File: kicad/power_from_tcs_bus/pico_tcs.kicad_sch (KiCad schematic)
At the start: 14 parts, among them J1 TCS In, J2 Conn_01x20_Male, J3 Conn_01x20_Male, J4 Keypad, J5 Display, U1 L7805, U2 ULN2003

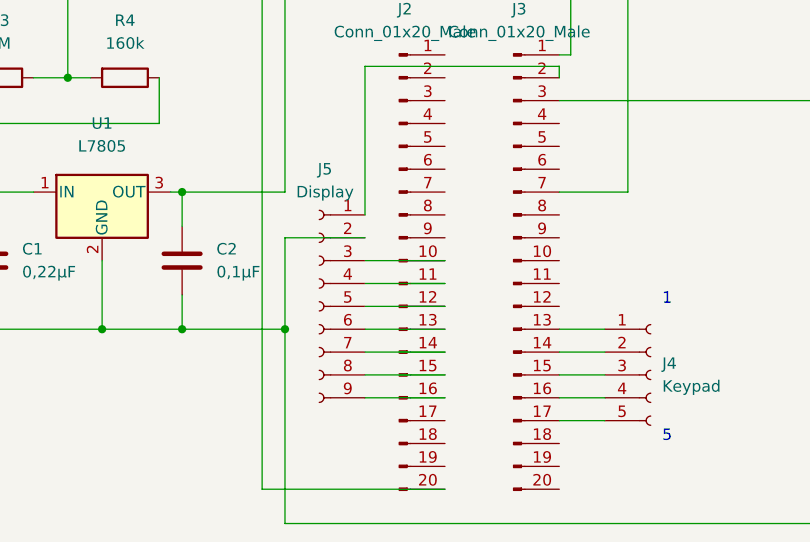
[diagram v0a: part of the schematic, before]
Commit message: Dateien hochladen nach „kicad/power_from_tcs_bus“
fixed bug in connection between display and pico
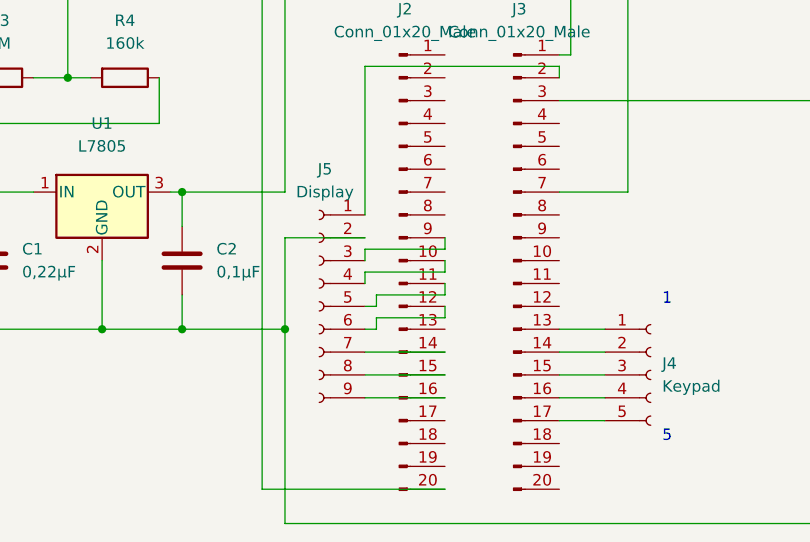
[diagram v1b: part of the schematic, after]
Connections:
- net at J5.3 (Pin_3): now also J2.9 (Pin_9); no longer J2.10 (Pin_10)
- net at J5.4 (Pin_4): now also J2.10 (Pin_10); no longer J2.11 (Pin_11)
- net at J5.5 (Pin_5): now also J2.11 (Pin_11); no longer J2.12 (Pin_12)
- net at J5.6 (Pin_6): now also J2.12 (Pin_12); no longer J2.13 (Pin_13)
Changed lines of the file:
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@@
+    (stroke (width 0) (type default) (color 0 0 0 0))
+  )
+  (wire (pts (xy 128.27 59.69) (xy 128.27 60.96))
     (stroke (width 0) (type default) (color 0 0 0 0))
   )
@@
   )
   (wire (pts (xy 110.49 69.85) (xy 99.06 69.85))
-    (stroke (width 0) (type default) (color 0 0 0 0))
-  )
-  (wire (pts (xy 119.38 69.85) (xy 128.27 69.85))
     (stroke (width 0) (type default) (color 0 0 0 0))
   )
@@
     (stroke (width 0) (type default) (color 0 0 0 0))
   )
+  (wire (pts (xy 119.38 77.47) (xy 128.27 77.47))
+    (stroke (width 0) (type default) (color 0 0 0 0))
+  )
   (wire (pts (xy 66.04 46.99) (xy 66.04 62.23))
     (stroke (width 0) (type default) (color 0 0 0 0))
   )
   (wire (pts (xy 66.04 62.23) (xy 71.12 62.23))
+    (stroke (width 0) (type default) (color 0 0 0 0))
+  )
+  (wire (pts (xy 119.38 69.85) (xy 120.65 69.85))
+    (stroke (width 0) (type default) (color 0 0 0 0))
+  )
+  (wire (pts (xy 119.38 64.77) (xy 119.38 63.5))
+    (stroke (width 0) (type default) (color 0 0 0 0))
+  )
+  (wire (pts (xy 119.38 74.93) (xy 128.27 74.93))
     (stroke (width 0) (type default) (color 0 0 0 0))
   )
@@
     (stroke (width 0) (type default) (color 0 0 0 0))
   )
-  (wire (pts (xy 119.38 62.23) (xy 128.27 62.23))
-    (stroke (width 0) (type default) (color 0 0 0 0))
-  )
   (wire (pts (xy 148.59 25.4) (xy 148.59 54.61))
     (stroke (width 0) (type default) (color 0 0 0 0))
@@
     (stroke (width 0) (type default) (color 0 0 0 0))
   )
-  (wire (pts (xy 119.38 72.39) (xy 128.27 72.39))
+  (wire (pts (xy 120.65 68.58) (xy 128.27 68.58))
     (stroke (width 0) (type default) (color 0 0 0 0))
   )
   (wire (pts (xy 54.61 25.4) (xy 64.77 25.4))
+    (stroke (width 0) (type default) (color 0 0 0 0))
+  )
+  (wire (pts (xy 128.27 64.77) (xy 128.27 66.04))
+    (stroke (width 0) (type default) (color 0 0 0 0))
+  )
+  (wire (pts (xy 119.38 63.5) (xy 128.27 63.5))
     (stroke (width 0) (type default) (color 0 0 0 0))
   )
@@
   )
   (wire (pts (xy 64.77 62.23) (xy 66.04 62.23))
+    (stroke (width 0) (type default) (color 0 0 0 0))
+  )
+  (wire (pts (xy 120.65 67.31) (xy 120.65 66.04))
     (stroke (width 0) (type default) (color 0 0 0 0))
   )
@@
     (stroke (width 0) (type default) (color 0 0 0 0))
   )
+  (wire (pts (xy 120.65 69.85) (xy 120.65 68.58))
+    (stroke (width 0) (type default) (color 0 0 0 0))
+  )
   (wire (pts (xy 96.52 41.91) (xy 96.52 46.99))
     (stroke (width 0) (type default) (color 0 0 0 0))
@@
     (stroke (width 0) (type default) (color 0 0 0 0))
   )
+  (wire (pts (xy 119.38 72.39) (xy 128.27 72.39))
+    (stroke (width 0) (type default) (color 0 0 0 0))
+  )
   (wire (pts (xy 119.38 40.64) (xy 140.97 40.64))
     (stroke (width 0) (type default) (color 0 0 0 0))
   )
-  (wire (pts (xy 119.38 77.47) (xy 128.27 77.47))
+  (wire (pts (xy 119.38 67.31) (xy 120.65 67.31))
     (stroke (width 0) (type default) (color 0 0 0 0))
   )
@@
     (stroke (width 0) (type default) (color 0 0 0 0))
   )
-  (wire (pts (xy 119.38 74.93) (xy 128.27 74.93))
-    (stroke (width 0) (type default) (color 0 0 0 0))
-  )
   (wire (pts (xy 16.51 31.75) (xy 27.94 31.75))
     (stroke (width 0) (type default) (color 0 0 0 0))
@@
     (stroke (width 0) (type default) (color 0 0 0 0))
   )
+  (wire (pts (xy 128.27 62.23) (xy 128.27 63.5))
+    (stroke (width 0) (type default) (color 0 0 0 0))
+  )
   (wire (pts (xy 168.91 44.45) (xy 140.97 44.45))
     (stroke (width 0) (type default) (color 0 0 0 0))
   )
-  (wire (pts (xy 119.38 64.77) (xy 128.27 64.77))
+  (wire (pts (xy 119.38 60.96) (xy 128.27 60.96))
     (stroke (width 0) (type default) (color 0 0 0 0))
   )
@@
     (stroke (width 0) (type default) (color 0 0 0 0))
   )
+  (wire (pts (xy 128.27 68.58) (xy 128.27 67.31))
+    (stroke (width 0) (type default) (color 0 0 0 0))
+  )
   (wire (pts (xy 110.49 91.44) (xy 168.91 91.44))
     (stroke (width 0) (type default) (color 0 0 0 0))
   )
-  (wire (pts (xy 119.38 67.31) (xy 128.27 67.31))
+  (wire (pts (xy 110.49 54.61) (xy 99.06 54.61))
     (stroke (width 0) (type default) (color 0 0 0 0))
   )
-  (wire (pts (xy 110.49 54.61) (xy 99.06 54.61))
+  (wire (pts (xy 120.65 66.04) (xy 128.27 66.04))
     (stroke (width 0) (type default) (color 0 0 0 0))
   )
@@
     (stroke (width 0) (type default) (color 0 0 0 0))
   )
+  (wire (pts (xy 119.38 62.23) (xy 119.38 60.96))
+    (stroke (width 0) (type default) (color 0 0 0 0))
+  )
